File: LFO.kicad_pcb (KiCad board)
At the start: 2 copper layers, 39.6 x 100 mm, 98 parts, among them J1 AudioJack2_SwitchT, J2 AudioJack2_SwitchT, J3 AudioJack2_SwitchT, J4 AudioJack2_SwitchT, J5 AudioJack2_SwitchT, J6 AudioJack2_SwitchT, J7 Conn_02x03_Odd_Even, J8 Conn_02x05_Odd_Even, Q1 BC847, SW1 SW_Push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

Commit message: Initial placement and power.
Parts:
- added R45: 100k, Resistor_SMD:R_0603_1608Metric, B.Cu at (152.4, 141.3)
- added R46: 220k, Resistor_SMD:R_0603_1608Metric, B.Cu at (152.4, 123.5)
- added R47: 220k, Resistor_SMD:R_0603_1608Metric, B.Cu at (152.4, 126.1)
- added U7: 74AHCT1G125, Package_TO_SOT_SMD:SOT-23-5, B.Cu at (153.6, 88.0)
- R19, R25, R31, R32, R33: value 68k -> 100k
- R28, R36: value 33k -> 47k
- R37: value 68k -> 47k
- RV2, RV4: footprint Local:AlpsRK09K -> Local:R09M3KT
- U3, U4: footprint Package_SO:MSOP-8_3x3mm_P0.65mm -> Package_DFN_QFN:DFN-8-1EP_3x2mm_P0.5mm_EP1.36x1.46mm
- U5: footprint Package_TO_SOT_SMD:TO-252-3_TabPin2 -> Package_TO_SOT_SMD:SOT-223-3_TabPin2
- U6: value LM324 -> LM324QT; footprint Package_DFN_QFN:QFN-16-1EP_3x3mm_P0.5mm_EP1.8x1.8mm -> Package_DFN_QFN:QFN-16-1EP_3x3mm_P0.5mm_EP1.7x1.7mm
- moved R32 53.2 mm to (152.4, 138.8), turned to 180 degrees
- moved R37 49.2 mm to (148.5, 131.0)
- moved SW1 36.8 mm to (146.2, 154.0)
- moved J3 30.6 mm to (140.9, 150.7), turned to 90 degrees
- moved R43 27.3 mm to (136.7, 90.0), turned to 180 degrees
- moved SW3 27.0 mm to (140.9, 84.7)
- moved R1 26.8 mm to (160.6, 90.0), turned to 180 degrees
- moved R41 26.1 mm to (136.7, 87.5), turned to 0 degrees
- moved C14 25.4 mm to (137.8, 76.2)
- moved R39 25.2 mm to (136.7, 84.9), turned to 180 degrees
- moved R25 25.0 mm to (152.4, 109.4), turned to 180 degrees
- moved C25 24.3 mm to (136.7, 82.3), turned to 0 degrees
- moved U5 24.3 mm to (150.5, 57.6), turned to 90 degrees
- moved J2 23.4 mm to (140.9, 135.5)
- moved R30 23.4 mm to (148.5, 114.8)
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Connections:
- C21 pad 2: Net-(C16-Pad1) -> Net-(C21-Pad2)
- J2 pad T: /OutputStage/Out -> /CVIn05.sch/In
- J2 pad TN: Net-(J2-PadTN) -> GND
- J3 pad T: /CVIn05.sch/In -> /DigitalIn/In
- J3 pad TN: GND -> +5V
- J4 pad T: /OutputStage/Inv -> /OutputStage/Out
- J5 pad T: /DigitalIn/In -> /OutputStage/Inv
- J5 pad TN: +5V -> Net-(J5-PadTN)
- J7 pad 1: MISO -> LED1
- R19 pad 1: Net-(C16-Pad1) -> /OutputStage/Out
- R20 pad 2: MOSI -> OUT
- R31 pad 1: Net-(C21-Pad1) -> /OutputStage/Inv
- R31 pad 2: Net-(C16-Pad1) -> Net-(C21-Pad2)
- R32 pad 2: +12V -> Net-(R25-Pad1)
- R33 pad 2: Net-(C16-Pad2) -> Net-(C21-Pad2)
- R37 pad 1: -12V -> GND
- R6 pad 1: TRIG -> LED2
- RV4 pad 1: Net-(R37-Pad2) -> -12V
- RV4 pad 3: Net-(R32-Pad1) -> +12V
- U1 pad 14: LED1 -> LED2
- U1 pad 20: MISO -> LED1
- U6 pad 1: Net-(C15-Pad1) -> Net-(R29-Pad1)
- U6 pad 10: Net-(C22-Pad1) -> (no net)
- U6 pad 15: (no net) -> Net-(C15-Pad1)
- U6 pad 16: (no net) -> Net-(C15-Pad2)
- U6 pad 2: Net-(C15-Pad2) -> +12V
- U6 pad 3: Net-(R29-Pad1) -> (no net)
- U6 pad 4: +12V -> Net-(R36-Pad2)
- U6 pad 5: Net-(R36-Pad2) -> Net-(C21-Pad2)
- U6 pad 6: Net-(C16-Pad1) -> Net-(C21-Pad1)
- U6 pad 7: Net-(C21-Pad1) -> Net-(R33-Pad1)
- U6 pad 8: Net-(R33-Pad1) -> Net-(R32-Pad1)
- U6 pad 9: Net-(R33-Pad1) -> Net-(R37-Pad2)
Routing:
- net +5V: track 303.7 -> 7.15 mm, vias 0 -> 1
- net Net-(C16-Pad2): track 79.9 -> 0.00 mm, vias 3 -> 0
- net RESET: track 67.1 -> 0.00 mm
- net Net-(C5-Pad1): track 65.0 -> 0.00 mm, vias 1 -> 0
- net SYNC: track 58.9 -> 0.00 mm, vias 2 -> 0
- net TRIG: track 58.1 -> 0.00 mm
- net Net-(C15-Pad1): track 52.5 -> 0.00 mm, vias 3 -> 0
- net FREQ: track 51.1 -> 0.00 mm, vias 2 -> 0
- net Net-(R38-Pad2): track 49.2 -> 0.00 mm
- net SCK: track 47.6 -> 0.00 mm
- net PWM: track 45.5 -> 0.00 mm
- net Net-(R29-Pad1): track 43.3 -> 0.00 mm, vias 3 -> 0
- net Net-(C22-Pad1): track 40.7 -> 0.00 mm, vias 1 -> 0
- net Net-(C16-Pad1): track 36.5 -> 0.00 mm, vias 3 -> 0
- net VRef-10: track 33.1 -> 0.00 mm, vias 2 -> 0
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- added copper zone on In1.Cu, net +5V
- added copper zone on In2.Cu, net GND
- removed copper zone on B.Cu, net GND
- removed copper zone on F.Cu, net GND
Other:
- board size 39.6 x 100 mm -> 29.5 x 106.5 mm
- copper layers 2 -> 4
- board text added: "Marangisto 2018, 2019"
- board text added: "Rev B"
- board text removed: "Marangisto 2018"
- board text removed: "Rev A"

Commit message: Some minor placement adjustments.
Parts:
- moved R44 19.3 mm to (144.6, 126.1)
- moved R47 17.2 mm to (160.4, 141.3), turned to 180 degrees
- moved R46 10.1 mm to (160.4, 117.3), turned to 180 degrees
- moved R28 8.76 mm to (152.4, 126.1), turned to 0 degrees
- moved R34 6.49 mm to (156.3, 136.2)
- moved R35 6.49 mm to (156.2, 138.8)
- moved R18 4.91 mm to (156.2, 126.1)
- moved R36 4.81 mm to (160.4, 131.0), turned to 180 degrees
- moved R26 4.58 mm to (156.2, 117.3), turned to 180 degrees
- moved R33 2.59 mm to (156.2, 141.4)
- moved C16 2.57 mm to (156.2, 121.0), turned to 0 degrees
- moved R27 2.57 mm to (156.2, 123.5)
- moved C21 2.49 mm to (156.2, 133.7)
- moved C23 2.34 mm to (160.4, 128.7)
- moved U6 0.25 mm to (156.0, 129.9)
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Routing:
- net -12V: track 169.8 -> 151.6 mm
- net +12V: track 100.2 -> 104.0 mm

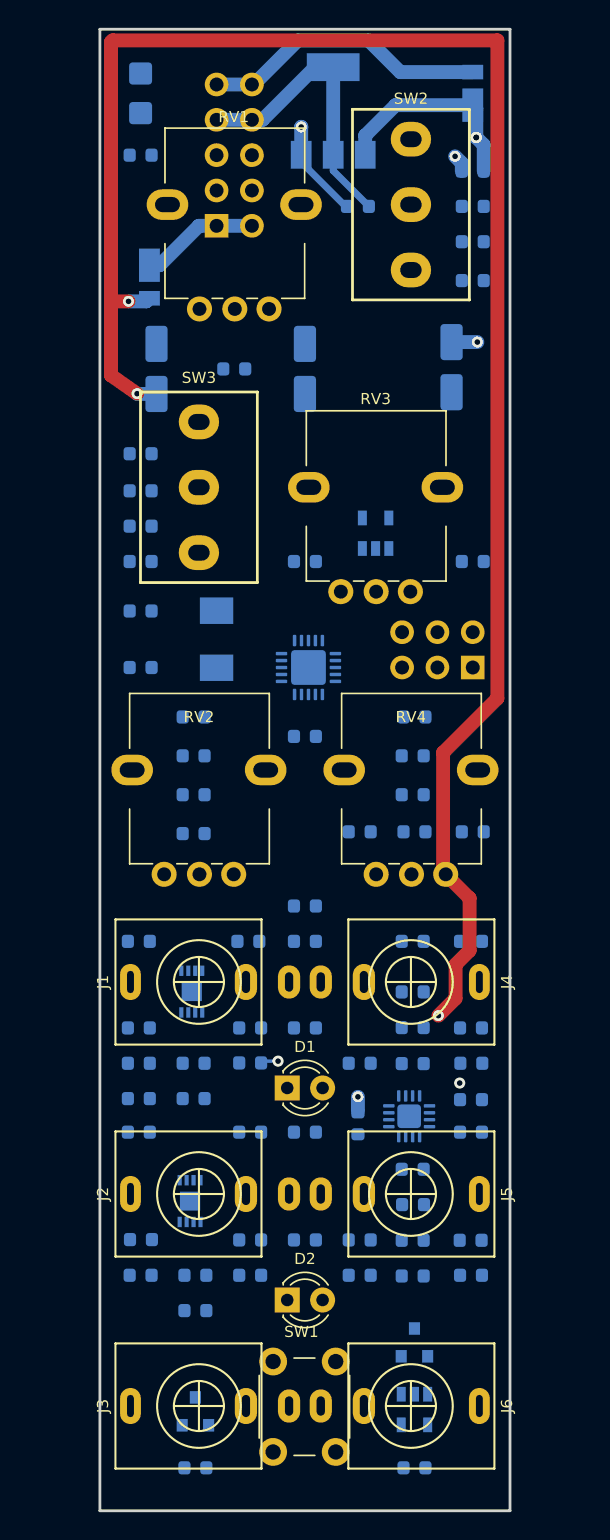
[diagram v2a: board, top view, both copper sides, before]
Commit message: Completed 4-layer routing.
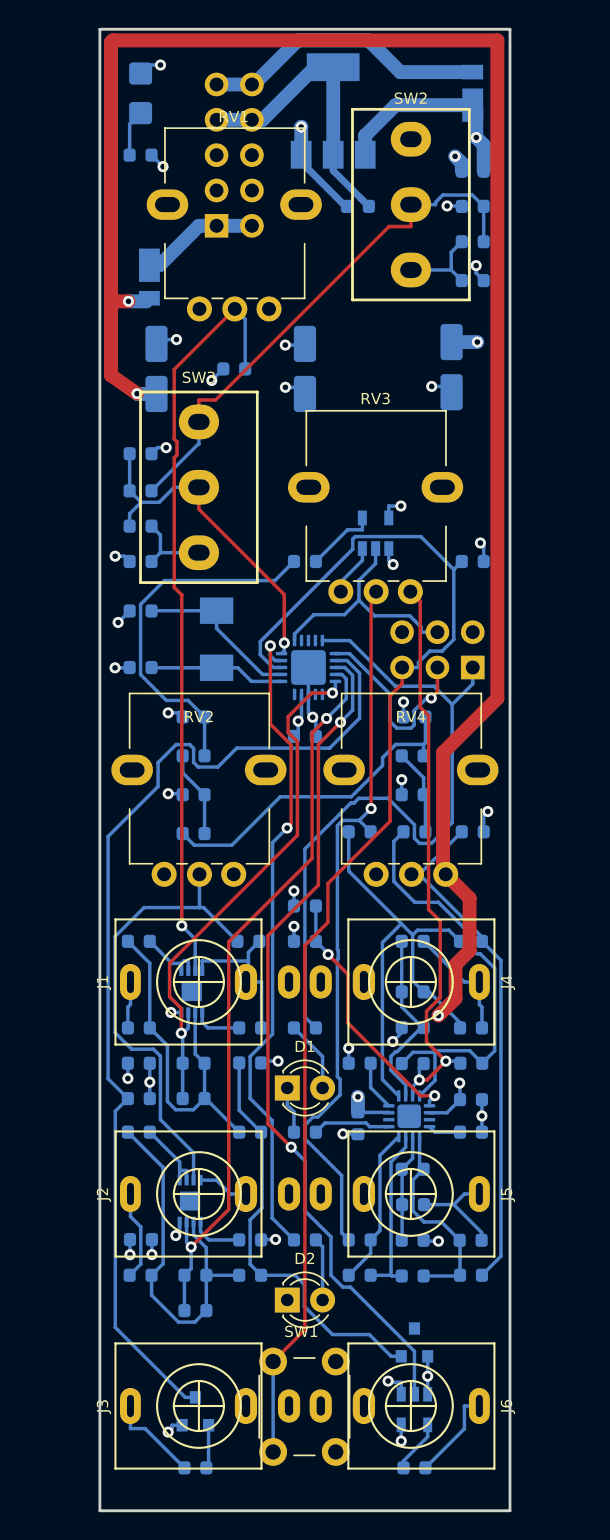
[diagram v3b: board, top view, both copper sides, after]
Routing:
- net RESET: track 0.00 -> 92.1 mm
- net SYNC: track 0.00 -> 74.0 mm
- net GND: track 22.3 -> 88.9 mm, vias 1 -> 30
- net TRIG: track 0.00 -> 60.4 mm, vias 0 -> 2
- net Net-(C5-Pad1): track 0.00 -> 54.8 mm, vias 0 -> 1
- net PWM: track 0.00 -> 53.1 mm, vias 0 -> 2
- net Net-(R25-Pad1): track 0.00 -> 52.3 mm, vias 0 -> 1
- net LED1: track 0.00 -> 50.8 mm
- net LED2: track 0.00 -> 47.5 mm, vias 0 -> 2
- net Net-(C15-Pad1): track 0.00 -> 41.8 mm, vias 0 -> 2
- net FREQ: track 0.00 -> 38.5 mm, vias 0 -> 2
- net Net-(R38-Pad2): track 0.00 -> 38.4 mm
- net Net-(C22-Pad1): track 0.00 -> 36.7 mm
- net Net-(C16-Pad2): track 0.00 -> 35.0 mm
- net Net-(C8-Pad1): track 0.00 -> 33.8 mm
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
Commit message: Autorouted 2-layer version but no power routing done.
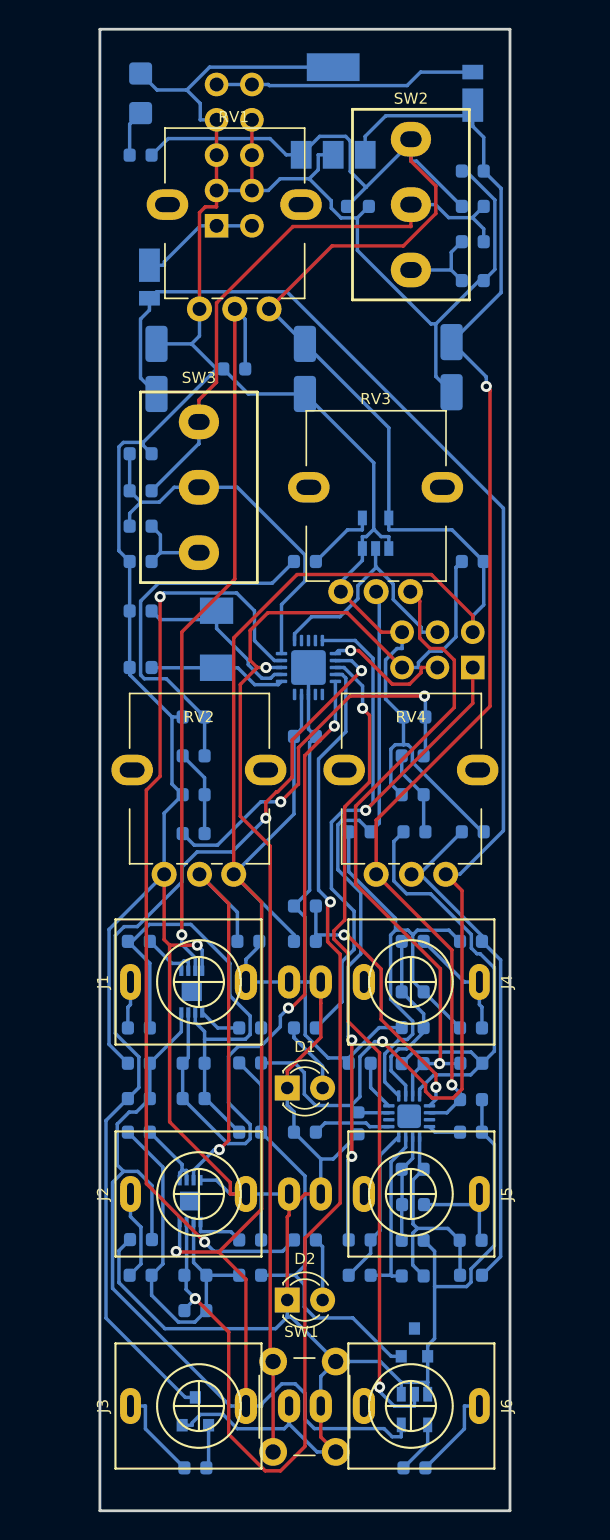
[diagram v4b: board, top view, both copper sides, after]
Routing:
- net GND: track 88.9 -> 408.3 mm, vias 30 -> 1
- net +5V: track 24.9 -> 250.0 mm, vias 13 -> 1
- net -12V: track 154.3 -> 109.6 mm, vias 5 -> 1
- net PWM: track 53.1 -> 83.9 mm
- net LED2: track 47.5 -> 67.7 mm
- net +12V: track 108.7 -> 93.1 mm, vias 3 -> 2
- net FREQ: track 38.5 -> 50.5 mm
- net Net-(C4-Pad2): track 25.9 -> 34.9 mm
- net RESET: track 92.1 -> 86.2 mm, vias 0 -> 1
- net SYNC: track 74.0 -> 68.6 mm, vias 0 -> 2
- net SCK: track 14.1 -> 9.13 mm
- net Net-(C15-Pad1): track 41.8 -> 46.6 mm, vias 2 -> 1
- net Net-(C19-Pad1): track 23.8 -> 28.1 mm, vias 0 -> 2
- net Net-(C8-Pad1): track 33.8 -> 30.1 mm, vias 0 -> 1
- net Net-(R38-Pad2): track 38.4 -> 41.3 mm
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- removed copper zone on In1.Cu, net +5V
- removed copper zone on In2.Cu, net GND
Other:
- copper layers 4 -> 2

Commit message: Revert "Autorouted 2-layer version but no power routing done."
This reverts commit d698285758b8106e3bcfe68091c579182fce5db9.
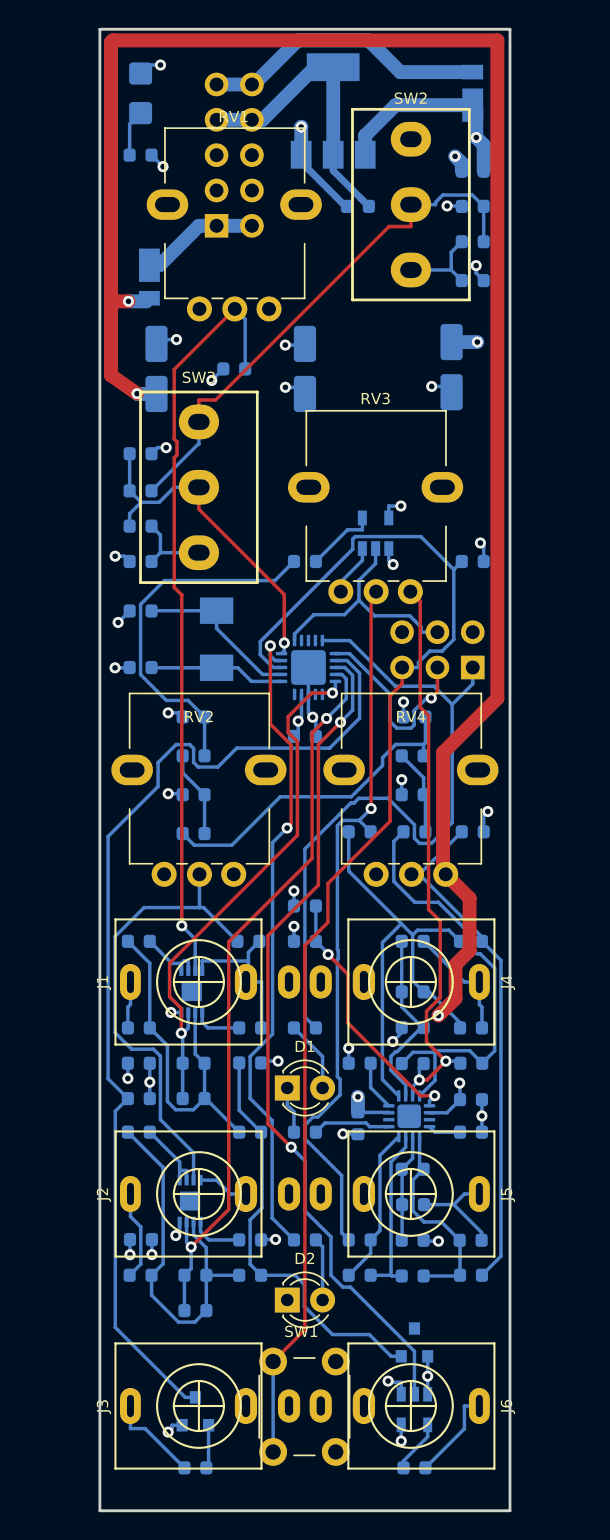
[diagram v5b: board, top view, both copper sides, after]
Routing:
- net GND: track 408.3 -> 88.9 mm, vias 1 -> 30
- net +5V: track 250.0 -> 24.9 mm, vias 1 -> 13
- net -12V: track 109.6 -> 154.3 mm, vias 1 -> 5
- net PWM: track 83.9 -> 53.1 mm
- net LED2: track 67.7 -> 47.5 mm
- net +12V: track 93.1 -> 108.7 mm, vias 2 -> 3
- net FREQ: track 50.5 -> 38.5 mm
- net Net-(C4-Pad2): track 34.9 -> 25.9 mm
- net RESET: track 86.2 -> 92.1 mm, vias 1 -> 0
- net SYNC: track 68.6 -> 74.0 mm, vias 2 -> 0
- net SCK: track 9.13 -> 14.1 mm
- net Net-(C15-Pad1): track 46.6 -> 41.8 mm, vias 1 -> 2
- net Net-(C19-Pad1): track 28.1 -> 23.8 mm, vias 2 -> 0
- net Net-(C8-Pad1): track 30.1 -> 33.8 mm, vias 1 -> 0
- net Net-(R38-Pad2): track 41.3 -> 38.4 mm
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- added copper zone on In1.Cu, net +5V
- added copper zone on In2.Cu, net GND
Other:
- copper layers 2 -> 4

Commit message: Added top and bottom pours.
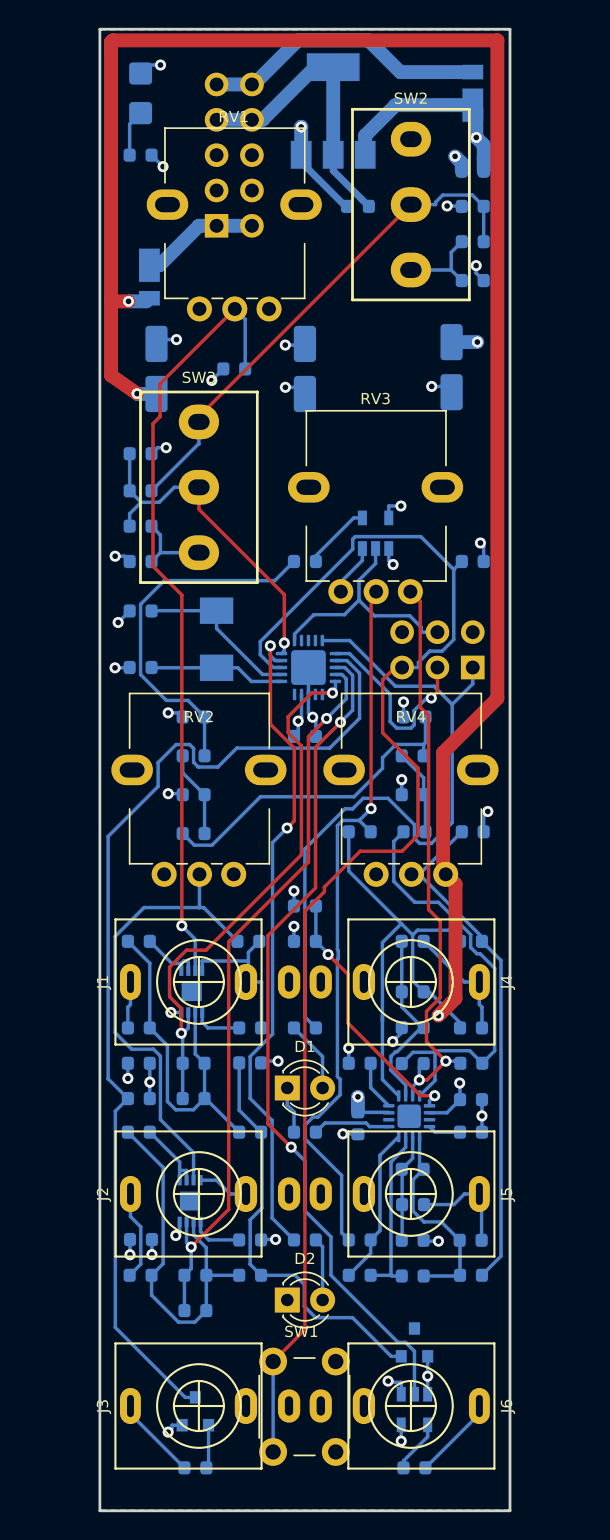
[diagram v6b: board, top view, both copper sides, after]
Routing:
- net RESET: track 92.1 -> 96.3 mm
- net Net-(R38-Pad2): track 38.4 -> 36.8 mm
- net Net-(C5-Pad1): track 54.8 -> 55.9 mm
- net FREQ: track 38.5 -> 39.5 mm
- net -12V: track 154.3 -> 153.4 mm
- net /OutputStage/Inv: track 7.69 -> 6.86 mm
- net /DigitalOut/Out: track 6.68 -> 6.05 mm
- net /DigitalIn/In: track 6.67 -> 6.05 mm
- added copper zone on B.Cu, net GND
- added copper zone on F.Cu, net GND
